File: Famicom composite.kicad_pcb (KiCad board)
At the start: 2 copper layers, 26 x 14.9 mm, 15 parts, among them J1 PPU_Pin21, J2 Conn_01x02, J3 Audio_In, J4 Conn_01x04_Female, U1 THS7314

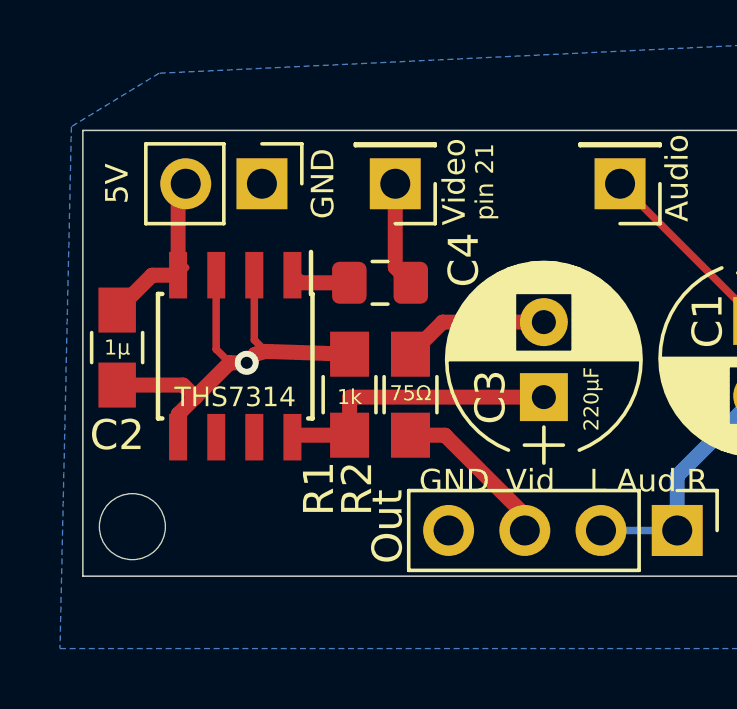
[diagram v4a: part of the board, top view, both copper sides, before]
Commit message: Add 3M input pullup pad
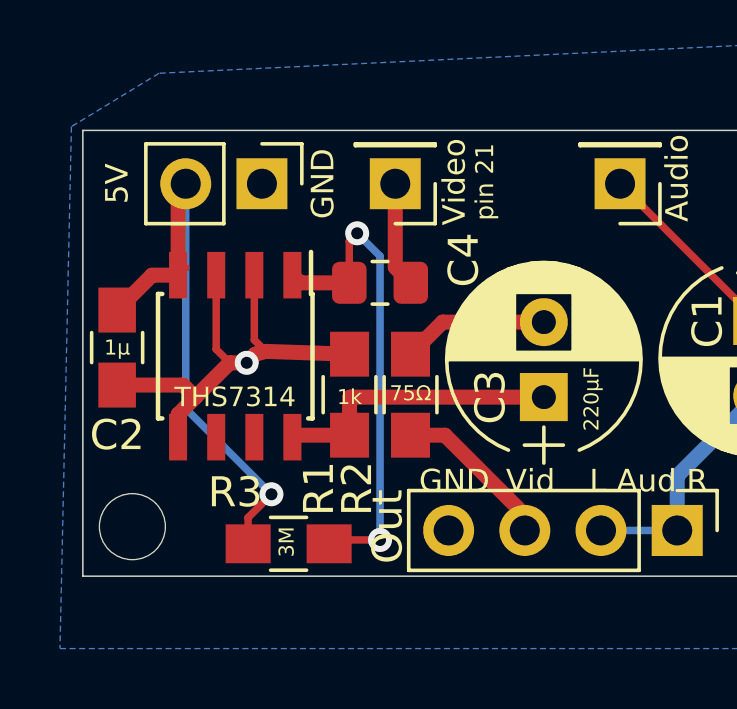
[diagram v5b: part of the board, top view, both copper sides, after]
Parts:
- added R3: 3MΩ, Resistors_SMD:R_0805_HandSoldering, F.Cu at (135.6, 97.9)
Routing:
- net Net-(C4-Pad1): track 2.00 -> 16.1 mm, vias 0 -> 2
- net +5V: track 6.15 -> 19.7 mm, vias 0 -> 1
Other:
- board text added: "3M"
- board text added: "famicom composite board v0.5"
- board text removed: "famicom composite board v0.4"
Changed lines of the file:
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@@
-(kicad_pcb (version 20171130) (host pcbnew "(5.1.5-0-10_14)")
+(kicad_pcb (version 20171130) (host pcbnew "(5.1.4-0-10_14)")
   (general
     (thickness 1.6)
-    (drawings 21)
-    (tracks 41)
+    (drawings 22)
+    (tracks 54)
     (zones 0)
-    (modules 15)
+    (modules 16)
     (nets 12)
   )
@@
   )
   (setup
-    (last_trace_width 0.5)
+    (last_trace_width 0.25)
     (user_trace_width 0.5)
     (trace_clearance 0.2)
@@
     (add_net "Net-(U1-Pad7)")
   )
-  (module Capacitor_SMD:C_0805_2012Metric_Pad1.15x1.40mm_HandSolder (layer F.Cu)
-    (at 138.684 89.154)
-    (descr "Capacitor SMD 0805 (2012 Metric), square (rectangular) end terminal, IPC_7351 nominal with elongated pad for handsoldering. (Body size source: https://docs.google.com/spreadsheets/d/1BsfQQcO9C6DZCsRaXUlFlo91Tg2WpOkGARC1WS5S8t0/edit?usp=sharing), generated with kicad-footprint-generator")
-    (tags "capacitor handsolder")
+  (module Resistors_SMD:R_0805_HandSoldering (layer F.Cu)
+    (at 135.636 97.8535 180)
+    (descr "Resistor SMD 0805, hand soldering")
+    (tags "resistor 0805")
     (attr smd)
-    (fp_text reference C4 (at 2.794 -0.762 90) (layer F.SilkS)
-      (effects (font (size 1 1) (thickness 0.15)))
-    )
-    (fp_text value 0.1µF (at 0 1.65) (layer F.Fab)
+    (fp_text reference R3 (at 1.778 1.7145) (layer F.SilkS)
+      (effects (font (size 1 1) (thickness 0.15)))
+    )
+    (fp_text value 3MΩ (at 0 1.75) (layer F.Fab)
       (effects (font (size 1 1) (thickness 0.15)))
     )
     (fp_text user %R (at 0 0) (layer F.Fab)
-      (effects (font (size 0.5 0.5) (thickness 0.08)))
-    )
-    (fp_line (start 1.85 0.95) (end -1.85 0.95) (layer F.CrtYd) (width 0.05))
-    (fp_line (start 1.85 -0.95) (end 1.85 0.95) (layer F.CrtYd) (width 0.05))
-    (fp_line (start -1.85 -0.95) (end 1.85 -0.95) (layer F.CrtYd) (width 0.05))
-    (fp_line (start -1.85 0.95) (end -1.85 -0.95) (layer F.CrtYd) (width 0.05))
-    (fp_line (start -0.261252 0.71) (end 0.261252 0.71) (layer F.SilkS) (width 0.12))
-    (fp_line (start -0.261252 -0.71) (end 0.261252 -0.71) (layer F.SilkS) (width 0.12))
-    (fp_line (start 1 0.6) (end -1 0.6) (layer F.Fab) (width 0.1))
-    (fp_line (start 1 -0.6) (end 1 0.6) (layer F.Fab) (width 0.1))
-    (fp_line (start -1 -0.6) (end 1 -0.6) (layer F.Fab) (width 0.1))
-    (fp_line (start -1 0.6) (end -1 -0.6) (layer F.Fab) (width 0.1))
-    (pad 2 smd roundrect (at 1.025 0) (size 1.15 1.4) (layers F.Cu F.Paste F.Mask) (roundrect_rratio 0.217391)
-      (net 10 "Net-(C4-Pad2)"))
-    (pad 1 smd roundrect (at -1.025 0) (size 1.15 1.4) (layers F.Cu F.Paste F.Mask) (roundrect_rratio 0.217391)
+      (effects (font (size 0.5 0.5) (thickness 0.075)))
+    )
+    (fp_line (start -1 0.62) (end -1 -0.62) (layer F.Fab) (width 0.1))
+    (fp_line (start 1 0.62) (end -1 0.62) (layer F.Fab) (width 0.1))
+    (fp_line (start 1 -0.62) (end 1 0.62) (layer F.Fab) (width 0.1))
+    (fp_line (start -1 -0.62) (end 1 -0.62) (layer F.Fab) (width 0.1))
+    (fp_line (start 0.6 0.88) (end -0.6 0.88) (layer F.SilkS) (width 0.12))
+    (fp_line (start -0.6 -0.88) (end 0.6 -0.88) (layer F.SilkS) (width 0.12))
+    (fp_line (start -2.35 -0.9) (end 2.35 -0.9) (layer F.CrtYd) (width 0.05))
+    (fp_line (start -2.35 -0.9) (end -2.35 0.9) (layer F.CrtYd) (width 0.05))
+    (fp_line (start 2.35 0.9) (end 2.35 -0.9) (layer F.CrtYd) (width 0.05))
+    (fp_line (start 2.35 0.9) (end -2.35 0.9) (layer F.CrtYd) (width 0.05))
+    (pad 1 smd rect (at -1.35 0 180) (size 1.5 1.3) (layers F.Cu F.Paste F.Mask)
       (net 11 "Net-(C4-Pad1)"))
-    (model ${KISYS3DMOD}/Capacitor_SMD.3dshapes/C_0805_2012Metric.wrl
+    (pad 2 smd rect (at 1.35 0 180) (size 1.5 1.3) (layers F.Cu F.Paste F.Mask)
+      (net 2 +5V))
+    (model ${KISYS3DMOD}/Resistors_SMD.3dshapes/R_0805.wrl
       (at (xyz 0 0 0))
       (scale (xyz 1 1 1))
@@
     )
   )
-  (module Symbols:OSHW-Logo2_9.8x8mm_SilkScreen (layer B.Cu)
+  (module Symbols:OSHW-Logo2_9.8x8mm_SilkScreen locked (layer B.Cu)
     (at 134.239 92.329 180)
     (descr "Open Source Hardware Symbol")
@@
       (xy -0.017575 3.712307) (xy 0 3.712308) (xy 0.139878 3.712224)) (layer B.SilkS) (width 0.01))
   )
-  (module Mounting_Holes:MountingHole_2.2mm_M2_DIN965 (layer F.Cu)
+  (module Mounting_Holes:MountingHole_2.2mm_M2_DIN965 locked (layer F.Cu)
     (at 130.429 97.282)
     (descr "Mounting Hole 2.2mm, no annular, M2, DIN965")
@@
     (pad 1 np_thru_hole circle (at 0 0) (size 2.2 2.2) (drill 2.2) (layers *.Cu *.Mask))
   )
-  (module Mounting_Holes:MountingHole_2.2mm_M2_DIN965 (layer F.Cu)
+  (module Mounting_Holes:MountingHole_2.2mm_M2_DIN965 locked (layer F.Cu)
     (at 153.162 97.282)
     (descr "Mounting Hole 2.2mm, no annular, M2, DIN965")
@@
     (pad 1 np_thru_hole circle (at 0 0) (size 2.2 2.2) (drill 2.2) (layers *.Cu *.Mask))
   )
-  (module Mounting_Holes:MountingHole_2.2mm_M2_DIN965 (layer F.Cu)
+  (module Mounting_Holes:MountingHole_2.2mm_M2_DIN965 locked (layer F.Cu)
     (at 153.162 85.725)
     (descr "Mounting Hole 2.2mm, no annular, M2, DIN965")
@@
     (fp_circle (center 0 0) (end 2.15 0) (layer F.CrtYd) (width 0.05))
     (pad 1 np_thru_hole circle (at 0 0) (size 2.2 2.2) (drill 2.2) (layers *.Cu *.Mask))
+  )
+  (module Capacitor_SMD:C_0805_2012Metric_Pad1.15x1.40mm_HandSolder (layer F.Cu)
+    (at 138.684 89.154)
+    (descr "Capacitor SMD 0805 (2012 Metric), square (rectangular) end terminal, IPC_7351 nominal with elongated pad for handsoldering. (Body size source: https://docs.google.com/spreadsheets/d/1BsfQQcO9C6DZCsRaXUlFlo91Tg2WpOkGARC1WS5S8t0/edit?usp=sharing), generated with kicad-footprint-generator")
+    (tags "capacitor handsolder")
+    (attr smd)
+    (fp_text reference C4 (at 2.794 -0.762 90) (layer F.SilkS)
+      (effects (font (size 1 1) (thickness 0.15)))
+    )
+    (fp_text value 0.1µF (at 0 1.65) (layer F.Fab)
+      (effects (font (size 1 1) (thickness 0.15)))
+    )
+    (fp_text user %R (at 0 0) (layer F.Fab)
+      (effects (font (size 0.5 0.5) (thickness 0.08)))
+    )
+    (fp_line (start 1.85 0.95) (end -1.85 0.95) (layer F.CrtYd) (width 0.05))
+    (fp_line (start 1.85 -0.95) (end 1.85 0.95) (layer F.CrtYd) (width 0.05))
+    (fp_line (start -1.85 -0.95) (end 1.85 -0.95) (layer F.CrtYd) (width 0.05))
+    (fp_line (start -1.85 0.95) (end -1.85 -0.95) (layer F.CrtYd) (width 0.05))
+    (fp_line (start -0.261252 0.71) (end 0.261252 0.71) (layer F.SilkS) (width 0.12))
+    (fp_line (start -0.261252 -0.71) (end 0.261252 -0.71) (layer F.SilkS) (width 0.12))
+    (fp_line (start 1 0.6) (end -1 0.6) (layer F.Fab) (width 0.1))
+    (fp_line (start 1 -0.6) (end 1 0.6) (layer F.Fab) (width 0.1))
+    (fp_line (start -1 -0.6) (end 1 -0.6) (layer F.Fab) (width 0.1))
+    (fp_line (start -1 0.6) (end -1 -0.6) (layer F.Fab) (width 0.1))
+    (pad 2 smd roundrect (at 1.025 0) (size 1.15 1.4) (layers F.Cu F.Paste F.Mask) (roundrect_rratio 0.217391)
+      (net 10 "Net-(C4-Pad2)"))
+    (pad 1 smd roundrect (at -1.025 0) (size 1.15 1.4) (layers F.Cu F.Paste F.Mask) (roundrect_rratio 0.217391)
+      (net 11 "Net-(C4-Pad1)"))
+    (model ${KISYS3DMOD}/Capacitor_SMD.3dshapes/C_0805_2012Metric.wrl
+      (at (xyz 0 0 0))
+      (scale (xyz 1 1 1))
+      (rotate (xyz 0 0 0))
+    )
   )
   (module Capacitors_ThroughHole:CP_Radial_D6.3mm_P2.50mm (layer F.Cu)
@@
     )
   )
-  (gr_text "famicom composite board v0.4" (at 142.494 88.392) (layer B.SilkS)
+  (gr_text 3M (at 135.5725 97.79 90) (layer F.SilkS)
+    (effects (font (size 0.5 0.5) (thickness 0.125)))
+  )
+  (gr_text "famicom composite board v0.5" (at 142.494 88.392) (layer B.SilkS)
     (effects (font (size 1 1) (thickness 0.15)) (justify mirror))
   )
@@
   (segment (start 131.953 86.106) (end 132.207 85.852) (width 0.5) (layer F.Cu) (net 2))
   (segment (start 131.953 88.9) (end 131.953 86.106) (width 0.5) (layer F.Cu) (net 2))
+  (via (at 135.0645 96.2025) (size 0.8) (drill 0.4) (layers F.Cu B.Cu) (net 2))
+  (segment (start 134.286 96.981) (end 135.0645 96.2025) (width 0.25) (layer F.Cu) (net 2))
+  (segment (start 134.286 97.8535) (end 134.286 96.981) (width 0.25) (layer F.Cu) (net 2))
+  (segment (start 132.207 93.345) (end 132.207 85.852) (width 0.25) (layer B.Cu) (net 2))
+  (segment (start 135.0645 96.2025) (end 132.207 93.345) (width 0.25) (layer B.Cu) (net 2))
   (segment (start 143.51 96.894) (end 143.51 97.409) (width 0.5) (layer F.Cu) (net 3))
   (segment (start 140.85 94.234) (end 143.51 96.894) (width 0.5) (layer F.Cu) (net 3))
@@
   (segment (start 136.017 89.154) (end 135.763 88.9) (width 0.5) (layer F.Cu) (net 11))
   (segment (start 137.659 89.154) (end 136.017 89.154) (width 0.5) (layer F.Cu) (net 11))
+  (via (at 137.922 87.503) (size 0.8) (drill 0.4) (layers F.Cu B.Cu) (net 11))
+  (segment (start 137.659 87.766) (end 137.922 87.503) (width 0.25) (layer F.Cu) (net 11))
+  (segment (start 137.659 89.154) (end 137.659 87.766) (width 0.25) (layer F.Cu) (net 11))
+  (via (at 138.684 97.7265) (size 0.8) (drill 0.4) (layers F.Cu B.Cu) (net 11))
+  (segment (start 138.684 88.265) (end 138.684 97.7265) (width 0.25) (layer B.Cu) (net 11))
+  (segment (start 137.922 87.503) (end 138.684 88.265) (width 0.25) (layer B.Cu) (net 11))
+  (segment (start 137.113 97.7265) (end 136.986 97.8535) (width 0.25) (layer F.Cu) (net 11))
+  (segment (start 138.684 97.7265) (end 137.113 97.7265) (width 0.25) (layer F.Cu) (net 11))
   (zone (net 1) (net_name GND) (layer B.Cu) (hatch edge 0.508)
     (connect_pads (clearance 0.508))

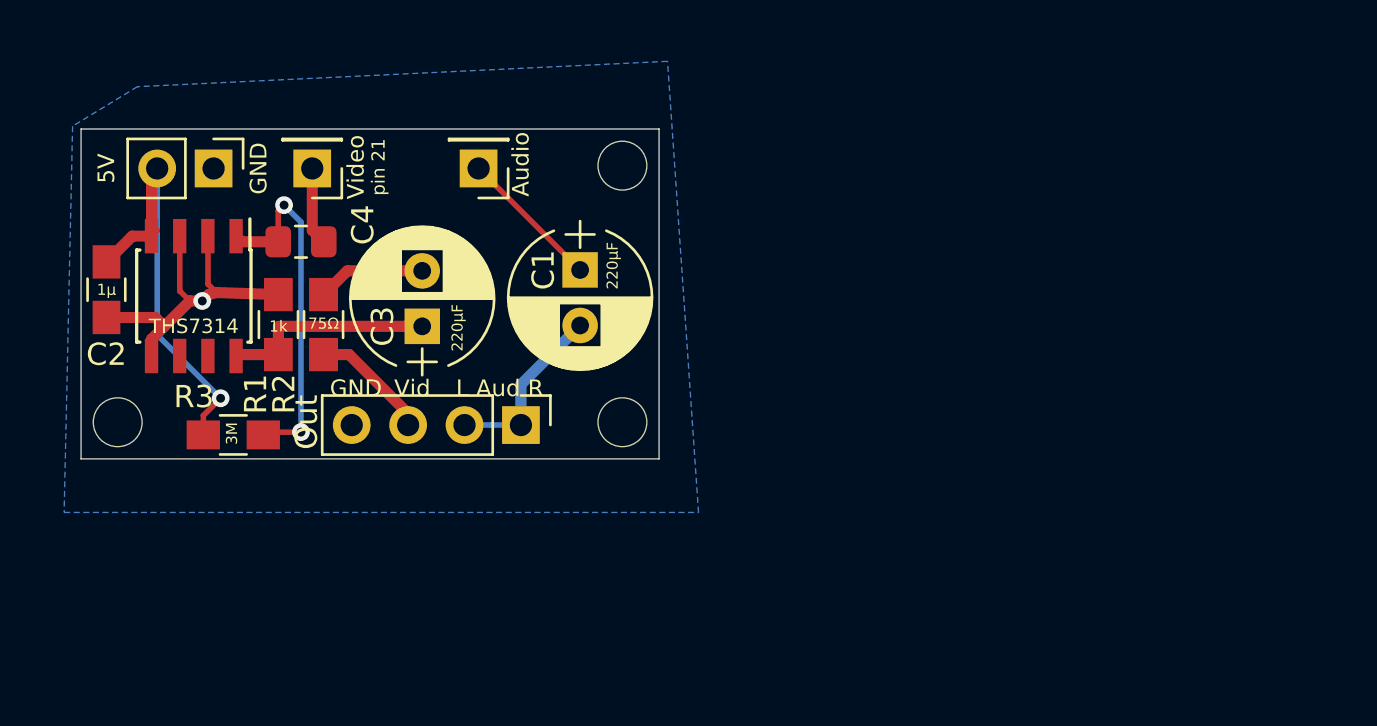
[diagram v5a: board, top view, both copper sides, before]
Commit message: Voltage divider variant
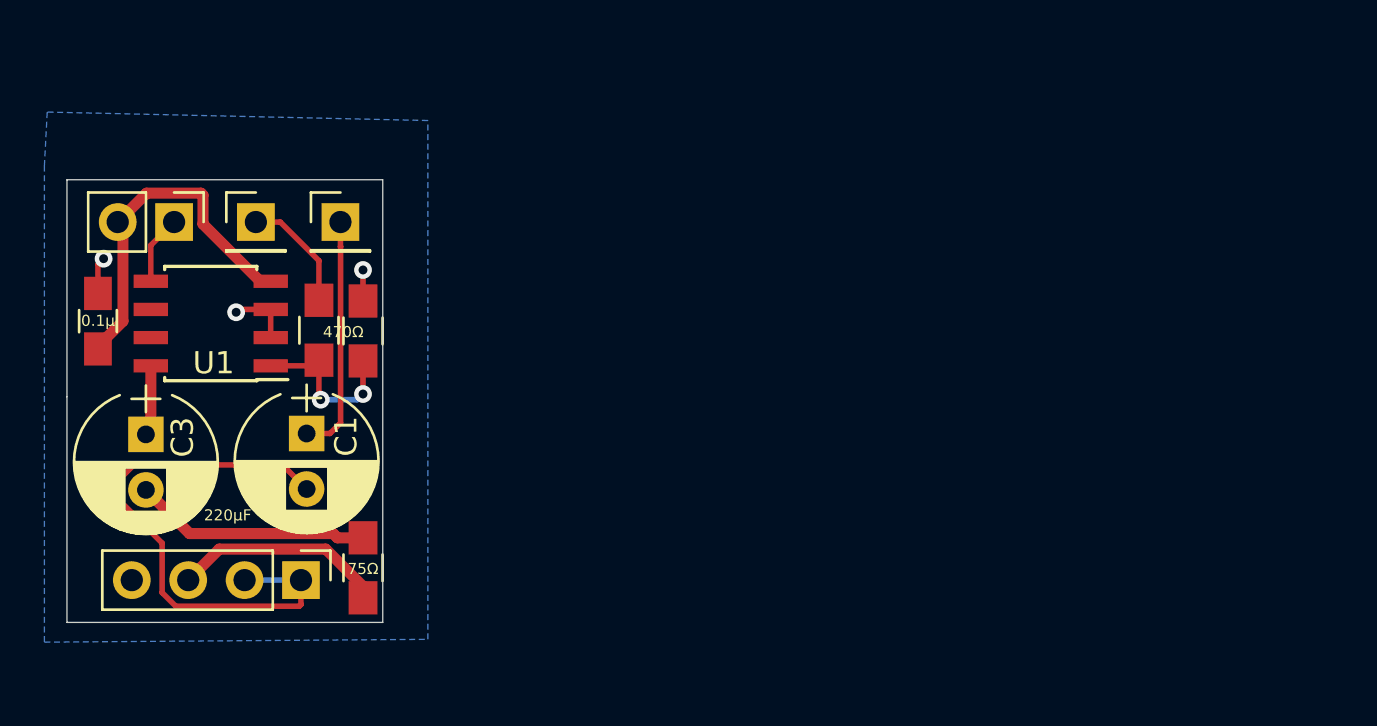
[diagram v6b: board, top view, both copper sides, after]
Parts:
- removed C4: 0.1µF, Capacitor_SMD:C_0805_2012Metric_Pad1.15x1.40mm_HandSolder
- removed REF** (x3): MountingHole_2.2mm_M2_DIN965, Mounting_Holes:MountingHole_2.2mm_M2_DIN965
- removed REF***: OSHW-Logo2_9.8x8mm_SilkScreen, Symbols:OSHW-Logo2_9.8x8mm_SilkScreen
- R1: value 1kΩ -> 470Ω
- R3: value 3MΩ -> 470Ω
- moved C1 14.4 mm to (138.9, 97.8)
- moved C3 13.4 mm to (131.7, 97.8), turned to 270 degrees
- moved J4 12.1 mm to (138.7, 104.4)
- moved R2 11.1 mm to (141.5, 103.8)
- moved R3 7.49 mm to (141.5, 93.2), turned to 90 degrees
- moved J3 6.67 mm to (140.5, 88.3), turned to 0 degrees
- moved J1 3.50 mm to (136.7, 88.3), turned to 0 degrees
- moved J2 3.00 mm to (133.0, 88.3)
- moved R1 1.84 mm to (139.5, 93.1)
- moved C2 1.47 mm to (129.5, 92.7), turned to 90 degrees
- moved U1 1.45 mm to (134.6, 92.8), turned to 180 degrees
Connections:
- J1 pad 1: Net-(C4-Pad2) -> Net-(J1-Pad1)
- R1 pad 1: GND -> Net-(J1-Pad1)
- R1 pad 2: Net-(C3-Pad1) -> /Half_Vpp
- R3 pad 1: Net-(C4-Pad1) -> /Half_Vpp
- R3 pad 2: +5V -> GND
- U1 pad 1: Net-(C4-Pad1) -> /Half_Vpp
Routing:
- net Net-(C1-Pad2): track 8.13 -> 25.2 mm
- net Net-(C4-Pad1): track 16.1 -> 0.00 mm, vias 2 -> 0
- net /Half_Vpp: track 0.00 -> 7.59 mm, vias 0 -> 2
- net GND: track 16.4 -> 9.05 mm, vias 1 -> 3
- net Net-(C3-Pad1): track 9.77 -> 3.18 mm
- net Net-(C3-Pad2): track 4.89 -> 10.7 mm
- net Net-(J1-Pad1): track 0.00 -> 5.34 mm
- net Net-(C1-Pad1): track 6.47 -> 10.8 mm
- net /Vid_Out: track 5.43 -> 9.66 mm
- net +5V: track 19.7 -> 16.1 mm, vias 1 -> 0
- net Net-(C4-Pad2): track 3.52 -> 0.00 mm
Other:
- board size 26 x 14.9 mm -> 14.2 x 19.9 mm
- board text added: "0.1µ"
- board text added: "470Ω"
- board text added: "Aud In"
- board text added: "Audio Out"
- board text added: "PPU pin21"
- board text added: "fami composite board v0.5"
- board text removed: "1k"
- board text removed: "1µ"
- board text removed: "3M"
- board text removed: "Audio"
- board text removed: "L Aud R"
- board text removed: "Out"
- board text removed: "THS7314"
- board text removed: "Video"
- board text removed: "famicom composite board v0.5"
- board text removed: "pin 21"

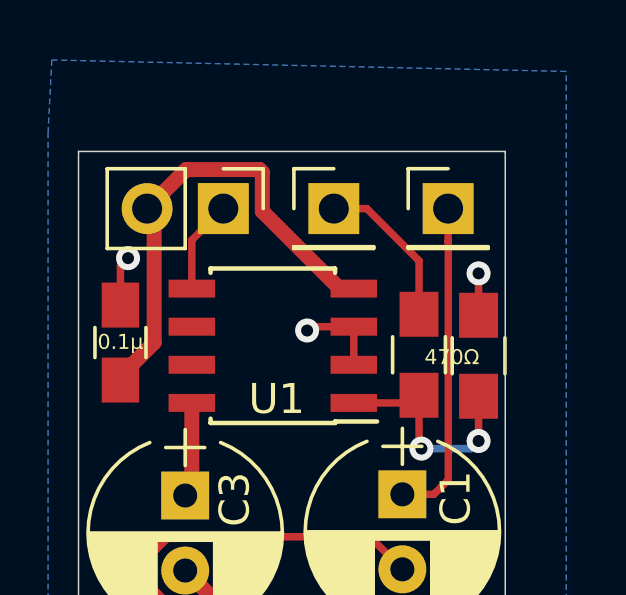
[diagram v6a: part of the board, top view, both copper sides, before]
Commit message: Label the dividers
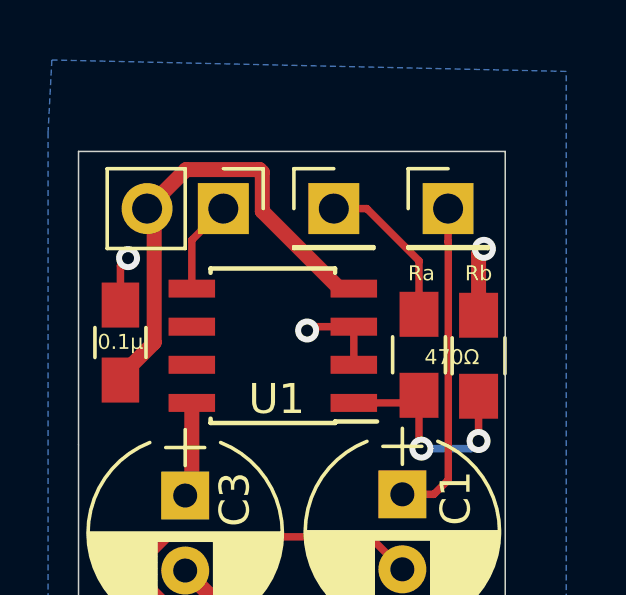
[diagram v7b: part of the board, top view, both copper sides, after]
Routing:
- net GND: track 9.05 -> 9.94 mm
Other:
- board text added: "Ra"
- board text added: "Rb"
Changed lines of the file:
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@@
-(kicad_pcb (version 20171130) (host pcbnew "(5.1.4-0-10_14)")
+(kicad_pcb (version 20171130) (host pcbnew "(5.1.5-0-10_14)")
   (general
     (thickness 1.6)
-    (drawings 18)
-    (tracks 59)
+    (drawings 20)
+    (tracks 60)
     (zones 0)
     (modules 11)
@@
   )
   (setup
-    (last_trace_width 0.25)
+    (last_trace_width 0.5)
     (user_trace_width 0.5)
     (trace_clearance 0.2)
@@
     )
   )
+  (gr_text Rb (at 141.478 90.424) (layer F.SilkS)
+    (effects (font (size 0.5 0.5) (thickness 0.125)))
+  )
+  (gr_text Ra (at 139.573 90.424) (layer F.SilkS)
+    (effects (font (size 0.5 0.5) (thickness 0.125)))
+  )
   (gr_text "leadedsolder.com 2020" (at 130.048 96.393 90) (layer B.SilkS)
     (effects (font (size 0.6 0.6) (thickness 0.15)) (justify mirror))
@@
     (effects (font (size 0.65 0.65) (thickness 0.15) italic) (justify mirror))
   )
-  (via (at 141.478 90.424) (size 0.8) (drill 0.4) (layers F.Cu B.Cu) (net 1))
-  (segment (start 141.478 91.821) (end 141.478 90.424) (width 0.25) (layer F.Cu) (net 1) (status 10))
   (via (at 135.763 92.329) (size 0.8) (drill 0.4) (layers F.Cu B.Cu) (net 1))
   (segment (start 135.89 92.202) (end 135.763 92.329) (width 0.25) (layer F.Cu) (net 1))
@@
   (segment (start 131.92 89.314) (end 132.969 88.265) (width 0.25) (layer F.Cu) (net 1) (status 20))
   (segment (start 131.92 90.932) (end 131.92 89.314) (width 0.25) (layer F.Cu) (net 1) (status 10))
+  (via (at 141.655292 89.607091) (size 0.8) (drill 0.4) (layers F.Cu B.Cu) (net 1))
+  (segment (start 141.478 89.784383) (end 141.655292 89.607091) (width 0.5) (layer F.Cu) (net 1))
+  (segment (start 141.478 91.821) (end 141.478 89.784383) (width 0.5) (layer F.Cu) (net 1))
   (segment (start 136.845 90.932) (end 137.32 90.932) (width 0.5) (layer F.Cu) (net 2) (status 30))
   (segment (start 134.269001 88.356001) (end 136.845 90.932) (width 0.5) (layer F.Cu) (net 2) (status 20))
